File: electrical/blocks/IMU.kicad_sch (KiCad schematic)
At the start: 3 parts, among them U1 LSM6DSOTR

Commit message: Relink blocks to Aerial library
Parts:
- C1, C2: value 100n -> 0u1; footprint rsx_capacitors:C_0603_1608Metric -> RSX_Aerial:C_0603_1608Metric; symbol rsx_Capacitors:10n -> RSX_Aerial_Capacitors:0u1; DPN 1276-1009-1-ND -> 445-1314-1-ND; MFR (none) -> TDK Corporation; MPN (none) -> C1608X7R1H104K080AA
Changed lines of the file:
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@@
 	)
 	(symbol
-		(lib_id "rsx_Capacitors:10n")
+		(lib_id "RSX_Aerial_Capacitors:0u1")
 		(at 67.31 101.6 0)
 		(unit 1)
@@
 			)
 		)
-		(property "Value" "100n"
+		(property "Value" "0u1"
 			(at 71.12 102.8699 0)
 			(show_name no)
@@
 			)
 		)
-		(property "Footprint" "rsx_capacitors:C_0603_1608Metric"
+		(property "Footprint" "RSX_Aerial:C_0603_1608Metric"
 			(at 68.2752 105.41 0)
 			(hide yes)
@@
 			)
 		)
-		(property "Datasheet" "https://mm.digikey.com/Volume0/opasdata/d220001/medias/docus/609/CL10B103KB8NNNC_Spec.pdf"
-			(at 67.31 101.6 0)
-			(hide yes)
-			(show_name no)
-			(do_not_autoplace no)
-			(effects
-				(font
-					(size 1.27 1.27)
-				)
-			)
-		)
-		(property "Description" "CAP CER 10000PF 50V X7R 0603"
-			(at 67.31 101.6 0)
-			(hide yes)
-			(show_name no)
-			(do_not_autoplace no)
-			(effects
-				(font
-					(size 1.27 1.27)
-				)
-			)
-		)
-		(property "DPN" "1276-1009-1-ND"
+		(property "Datasheet" "~"
+			(at 67.31 101.6 0)
+			(hide yes)
+			(show_name no)
+			(do_not_autoplace no)
+			(effects
+				(font
+					(size 1.27 1.27)
+				)
+			)
+		)
+		(property "Description" "CAP CER 0.1UF 50V X7R 0603"
+			(at 67.31 101.6 0)
+			(hide yes)
+			(show_name no)
+			(do_not_autoplace no)
+			(effects
+				(font
+					(size 1.27 1.27)
+				)
+			)
+		)
+		(property "DPN" "445-1314-1-ND"
+			(at 67.31 101.6 0)
+			(hide yes)
+			(show_name no)
+			(do_not_autoplace no)
+			(effects
+				(font
+					(size 1.27 1.27)
+				)
+			)
+		)
+		(property "MFR" "TDK Corporation"
+			(at 67.31 101.6 0)
+			(hide yes)
+			(show_name no)
+			(do_not_autoplace no)
+			(effects
+				(font
+					(size 1.27 1.27)
+				)
+			)
+		)
+		(property "MPN" "C1608X7R1H104K080AA"
 			(at 67.31 101.6 0)
 			(hide yes)
@@
 	)
 	(symbol
-		(lib_id "rsx_Capacitors:10n")
+		(lib_id "RSX_Aerial_Capacitors:0u1")
 		(at 138.43 106.68 0)
 		(unit 1)
@@
 			)
 		)
-		(property "Value" "100n"
+		(property "Value" "0u1"
 			(at 142.24 107.9499 0)
 			(show_name no)
@@
 			)
 		)
-		(property "Footprint" "rsx_capacitors:C_0603_1608Metric"
+		(property "Footprint" "RSX_Aerial:C_0603_1608Metric"
 			(at 139.3952 110.49 0)
 			(hide yes)
@@
 			)
 		)
-		(property "Datasheet" "https://mm.digikey.com/Volume0/opasdata/d220001/medias/docus/609/CL10B103KB8NNNC_Spec.pdf"
-			(at 138.43 106.68 0)
-			(hide yes)
-			(show_name no)
-			(do_not_autoplace no)
-			(effects
-				(font
-					(size 1.27 1.27)
-				)
-			)
-		)
-		(property "Description" "CAP CER 10000PF 50V X7R 0603"
-			(at 138.43 106.68 0)
-			(hide yes)
-			(show_name no)
-			(do_not_autoplace no)
-			(effects
-				(font
-					(size 1.27 1.27)
-				)
-			)
-		)
-		(property "DPN" "1276-1009-1-ND"
-			(at 138.43 106.68 0)
-			(hide yes)
+		(property "Datasheet" "~"
+			(at 138.43 106.68 0)
+			(hide yes)
+			(show_name no)
+			(do_not_autoplace no)
+			(effects
+				(font
+					(size 1.27 1.27)
+				)
+			)
+		)
+		(property "Description" "CAP CER 0.1UF 50V X7R 0603"
+			(at 138.43 106.68 0)
+			(hide yes)
+			(show_name no)
+			(do_not_autoplace no)
+			(effects
+				(font
+					(size 1.27 1.27)
+				)
+			)
+		)
+		(property "DPN" "445-1314-1-ND"
+			(at 138.43 106.68 0)
+			(hide yes)
+			(show_name no)
+			(do_not_autoplace no)
+			(effects
+				(font
+					(size 1.27 1.27)
+				)
+			)
+		)
+		(property "MFR" "TDK Corporation"
+			(at 138.43 106.68 0)
+			(hide yes)
+			(show_name no)
+			(do_not_autoplace no)
+			(effects
+				(font
+					(size 1.27 1.27)
+				)
+			)
+		)
+		(property "MPN" "C1608X7R1H104K080AA"
+			(at 138.43 106.68 0)
+			(hide yes)

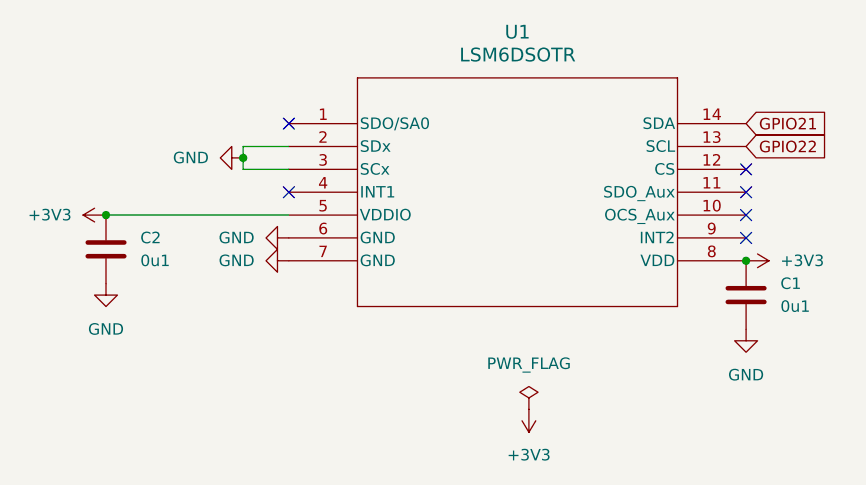
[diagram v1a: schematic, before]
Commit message: Edit IMU schematic
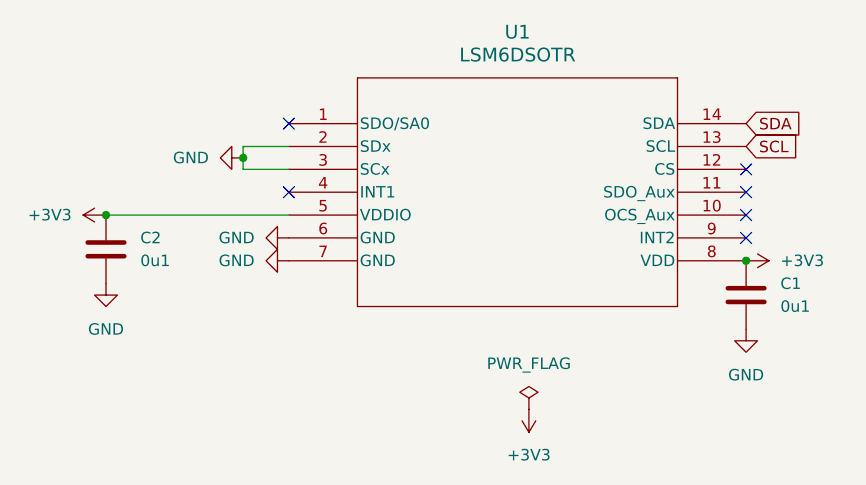
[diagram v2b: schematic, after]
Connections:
- net GPIO21 renamed SDA
- net GPIO22 renamed SCL
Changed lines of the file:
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@@
 		)
 	)
-	(global_label "GPIO21"
+	(global_label "SDA"
 		(shape input)
 		(at 138.43 87.63 0)
@@
 		)
 		(property "Intersheetrefs" "${INTERSHEET_REFS}"
-			(at 148.3095 87.63 0)
+			(at 144.9833 87.63 0)
 			(hide yes)
 			(show_name no)
@@
 		)
 	)
-	(global_label "GPIO22"
+	(global_label "SCL"
 		(shape input)
 		(at 138.43 90.17 0)
@@
 		)
 		(property "Intersheetrefs" "${INTERSHEET_REFS}"
-			(at 148.3095 90.17 0)
+			(at 144.9228 90.17 0)
 			(hide yes)
 			(show_name no)

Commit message: Edit IMU schematic
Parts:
- U1: footprint LGA-14L_2P5X3X0P86_STM -> RSX_Aerial:LGA-14L_2P5X3X0P86_STM; symbol Device:LSM6DSOTR -> RSX_Aerial:LSM6DSOTR; DPN (none) -> 497-18181-1-ND; MFR (none) -> STMicroelectronics; MPN (none) -> LSM6DSOTR
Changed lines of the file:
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@@
 	)
 	(symbol
-		(lib_id "Device:LSM6DSOTR")
+		(lib_id "RSX_Aerial:LSM6DSOTR")
 		(at 87.63 87.63 0)
 		(unit 1)
@@
 			)
 		)
-		(property "Footprint" "LGA-14L_2P5X3X0P86_STM"
+		(property "Footprint" "RSX_Aerial:LGA-14L_2P5X3X0P86_STM"
 			(at 87.63 87.63 0)
 			(hide yes)
@@
 			)
 		)
-		(property "Description" ""
+		(property "Description" "Accelerometer, Gyroscope, 6 Axis Sensor I2C, SPI Output"
 			(at 87.63 87.63 0)
 			(hide yes)
+			(show_name no)
+			(do_not_autoplace no)
+			(effects
+				(font
+					(size 1.27 1.27)
+				)
+			)
+		)
+		(property "MFR" "STMicroelectronics"
+			(at 87.63 87.63 0)
+			(hide yes)
+			(show_name no)
+			(do_not_autoplace no)
+			(effects
+				(font
+					(size 1.27 1.27)
+				)
+			)
+		)
+		(property "MPN" "LSM6DSOTR"
+			(at 87.63 87.63 0)
+			(hide yes)
+			(show_name no)
+			(do_not_autoplace no)
+			(effects
+				(font
+					(size 1.27 1.27)
+				)
+			)
+		)
+		(property "DPN" "497-18181-1-ND"
+			(at 87.63 87.63 0)
+			(hide yes)
